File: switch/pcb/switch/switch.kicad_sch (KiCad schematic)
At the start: 29 parts, among them J1 Conn_01x02_Female, SW1 SW_MEC_5G, U1 LNK304D

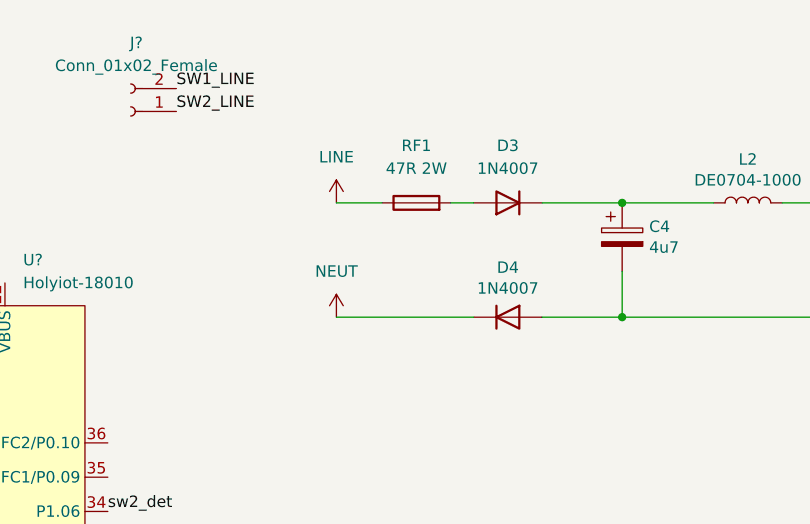
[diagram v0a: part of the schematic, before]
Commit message: switch: Add feature to set number of heartbeat pulses through CoAP
It is needed to disable heartbeats while debuggin hardware in production.
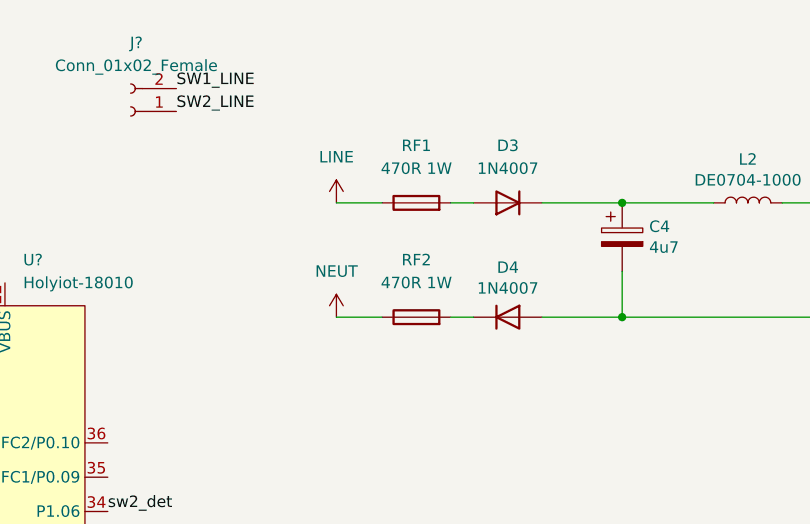
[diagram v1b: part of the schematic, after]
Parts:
- added RF2: 470R 1W, symbol Device:Fuse
- RF1: value 47R 2W -> 470R 1W
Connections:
- net NEUT: now also RF2.1; no longer D4.1 (K)
- new net: D4.1 (K), RF2.2

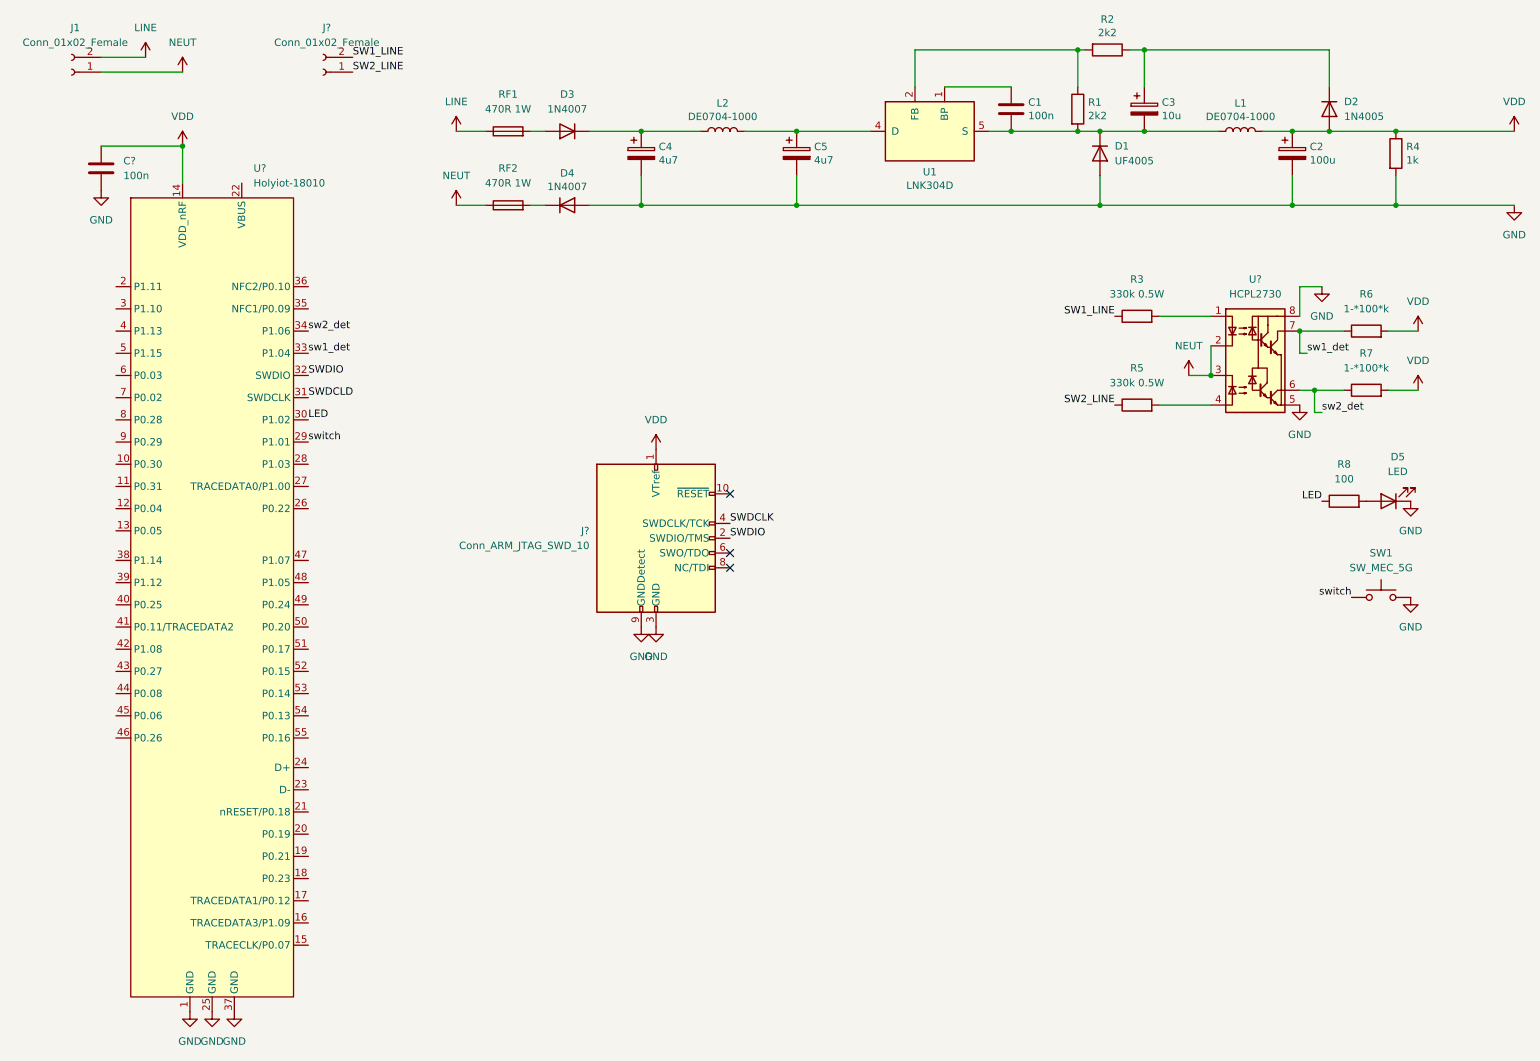
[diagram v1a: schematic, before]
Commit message: switch: Use ADC as an alternate switch detection
It looks some light switches do not disconnect electrical circuit but
increase their impedance instead. Impedance is low enough to keep
transoptor active, but with lower intensity than when the switch is
on. Transoptor intensity is detected with ADC and changes in intensity
treated as switch events.
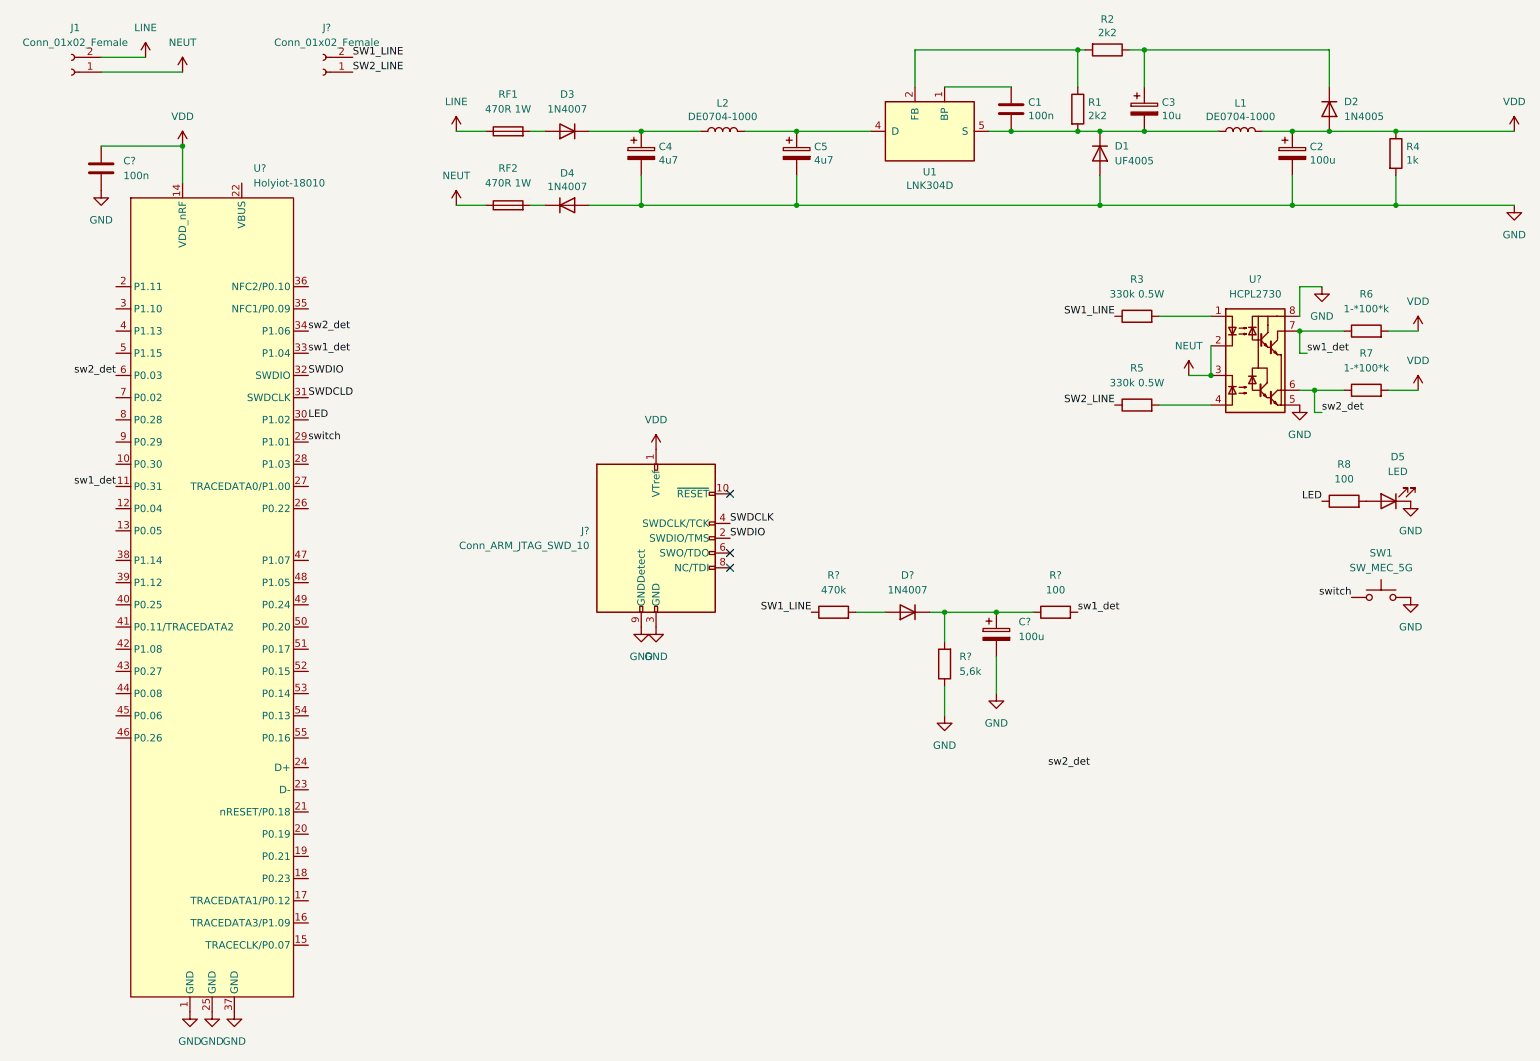
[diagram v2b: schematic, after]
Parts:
- added C?: 100u, symbol Device:C_Polarized
- added D?: 1N4007, symbol Device:D
- added R?: 5,6k, symbol Device:R
- added R?: 470k, symbol Device:R
- added R?: 100, symbol Device:R
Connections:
- net GND: now also C?.2, R?.1
- net SW1_LINE: now also R?.1
- net sw1_det: now also U?.11 (P0.31), R?.2
- net sw2_det: now also U?.6 (P0.03)
- new net: C?.1, D?.1 (K), R?.1, R?.2
- new net: D?.2 (A), R?.2
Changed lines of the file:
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@@
   (junction (at 252.73 36.83) (diameter 0) (color 0 0 0 0)
   )
+  (junction (at 175.26 119.38) (diameter 0) (color 0 0 0 0)
+  )
   (junction (at 201.93 36.83) (diameter 0) (color 0 0 0 0)
   )
@@
   )
   (junction (at 234.95 49.53) (diameter 0) (color 0 0 0 0)
+  )
+  (junction (at 184.15 119.38) (diameter 0) (color 0 0 0 0)
   )
   (junction (at 123.19 49.53) (diameter 0) (color 0 0 0 0)
@@
   (no_connect (at 138.43 111.76))
   (no_connect (at 138.43 109.22))
+  (wire (pts (xy 175.26 119.38) (xy 175.26 124.46))
+    (stroke (width 0) (type default) (color 0 0 0 0))
+  )
   (wire (pts (xy 240.03 85.09) (xy 238.76 85.09))
     (stroke (width 0) (type default) (color 0 0 0 0))
@@
     (stroke (width 0) (type default) (color 0 0 0 0))
   )
+  (wire (pts (xy 184.15 119.38) (xy 190.5 119.38))
+    (stroke (width 0) (type default) (color 0 0 0 0))
+  )
+  (wire (pts (xy 172.72 119.38) (xy 175.26 119.38))
+    (stroke (width 0) (type default) (color 0 0 0 0))
+  )
   (wire (pts (xy 234.95 36.83) (xy 241.3 36.83))
     (stroke (width 0) (type default) (color 0 0 0 0))
@@
     (stroke (width 0) (type default) (color 0 0 0 0))
   )
+  (wire (pts (xy 175.26 119.38) (xy 184.15 119.38))
+    (stroke (width 0) (type default) (color 0 0 0 0))
+  )
   (wire (pts (xy 252.73 36.83) (xy 273.05 36.83))
     (stroke (width 0) (type default) (color 0 0 0 0))
@@
     (stroke (width 0) (type default) (color 0 0 0 0))
   )
+  (wire (pts (xy 160.02 119.38) (xy 165.1 119.38))
+    (stroke (width 0) (type default) (color 0 0 0 0))
+  )
   (wire (pts (xy 186.69 36.83) (xy 198.12 36.83))
     (stroke (width 0) (type default) (color 0 0 0 0))
@@
     (stroke (width 0) (type default) (color 0 0 0 0))
   )
+  (wire (pts (xy 184.15 127) (xy 184.15 133.35))
+    (stroke (width 0) (type default) (color 0 0 0 0))
+  )
   (wire (pts (xy 234.95 44.45) (xy 234.95 49.53))
     (stroke (width 0) (type default) (color 0 0 0 0))
@@
     (stroke (width 0) (type default) (color 0 0 0 0))
   )
+  (wire (pts (xy 175.26 132.08) (xy 175.26 137.16))
+    (stroke (width 0) (type default) (color 0 0 0 0))
+  )
   (wire (pts (xy 114.3 49.53) (xy 123.19 49.53))
     (stroke (width 0) (type default) (color 0 0 0 0))
@@
   (wire (pts (xy 201.93 49.53) (xy 234.95 49.53))
     (stroke (width 0) (type default) (color 0 0 0 0))
+  )
+  (label "SW1_LINE" (at 152.4 119.38 180)
+    (effects (font (size 1.27 1.27)) (justify right bottom))
   )
   (label "SWDIO" (at 138.43 106.68 0)
     (effects (font (size 1.27 1.27)) (justify left bottom))
   )
+  (label "sw2_det" (at 193.04 146.05 0)
+    (effects (font (size 1.27 1.27)) (justify left bottom))
+  )
   (label "SW1_LINE" (at 204.47 68.58 180)
     (effects (font (size 1.27 1.27)) (justify right bottom))
@@
     (effects (font (size 1.27 1.27)) (justify left bottom))
   )
+  (label "sw2_det" (at 33.02 78.74 180)
+    (effects (font (size 1.27 1.27)) (justify right bottom))
+  )
   (label "sw1_det" (at 237.49 74.93 0)
     (effects (font (size 1.27 1.27)) (justify left bottom))
@@
     (effects (font (size 1.27 1.27)) (justify right bottom))
   )
+  (label "sw1_det" (at 33.02 97.79 180)
+    (effects (font (size 1.27 1.27)) (justify right bottom))
+  )
   (label "SW2_LINE" (at 204.47 83.82 180)
     (effects (font (size 1.27 1.27)) (justify right bottom))
+  )
+  (label "sw1_det" (at 198.12 119.38 0)
+    (effects (font (size 1.27 1.27)) (justify left bottom))
   )
   (label "switch" (at 66.04 90.17 0)
@@
     (pin "1")
   )
+  (symbol (lib_id "Device:D") (at 168.91 119.38 180) (unit 1)
+    (in_bom yes) (on_board yes) (fields_autoplaced)
+    (property "Reference" "D?" (id 0) (at 168.91 113.03 0))
+    (property "Value" "1N4007" (id 1) (at 168.91 115.57 0))
+    (property "Footprint" "" (id 2) (at 168.91 119.38 0)
+      (effects (font (size 1.27 1.27)) hide)
+    )
+    (property "Datasheet" "~" (id 3) (at 168.91 119.38 0)
+      (effects (font (size 1.27 1.27)) hide)
+    )
+    (pin "1")
+    (pin "2")
+  )
   (symbol (lib_id "Switch:SW_MEC_5G") (at 250.19 116.84 0) (unit 1)
     (in_bom yes) (on_board yes) (fields_autoplaced)
@@
     (pin "1")
   )
+  (symbol (lib_id "Device:R") (at 175.26 128.27 180) (unit 1)
+    (in_bom yes) (on_board yes) (fields_autoplaced)
+    (property "Reference" "R?" (id 0) (at 177.8 126.9999 0)
+      (effects (font (size 1.27 1.27)) (justify right))
+    )
+    (property "Value" "5,6k" (id 1) (at 177.8 129.5399 0)
+      (effects (font (size 1.27 1.27)) (justify right))
+    )
+    (property "Footprint" "" (id 2) (at 177.038 128.27 90)
+      (effects (font (size 1.27 1.27)) hide)
+    )
+    (property "Datasheet" "~" (id 3) (at 175.26 128.27 0)
+      (effects (font (size 1.27 1.27)) hide)
+    )
+    (pin "1")
+    (pin "2")
+  )
   (symbol (lib_id "Device:R") (at 208.28 68.58 90) (unit 1)
     (in_bom yes) (on_board yes) (fields_autoplaced)
@@
     )
     (property "Datasheet" "~" (id 3) (at 252.73 40.64 0)
+      (effects (font (size 1.27 1.27)) hide)
+    )
+    (pin "1")
+    (pin "2")
+  )
+  (symbol (lib_id "Device:C_Polarized") (at 184.15 123.19 0) (unit 1)
+    (in_bom yes) (on_board yes)
+    (property "Reference" "C?" (id 0) (at 187.96 121.0309 0)
+      (effects (font (size 1.27 1.27)) (justify left))
+    )
+    (property "Value" "100u" (id 1) (at 187.96 123.5709 0)
+      (effects (font (size 1.27 1.27)) (justify left))
+    )
+    (property "Footprint" "" (id 2) (at 185.1152 127 0)
+      (effects (font (size 1.27 1.27)) hide)
+    )
+    (property "Datasheet" "~" (id 3) (at 184.15 123.19 0)
       (effects (font (size 1.27 1.27)) hide)
     )
@@
     (pin "2")
   )
+  (symbol (lib_id "power:GND") (at 184.15 133.35 0) (unit 1)
+    (in_bom yes) (on_board yes)
+    (property "Reference" "#PWR?" (id 0) (at 184.15 139.7 0)
+      (effects (font (size 1.27 1.27)) hide)
+    )
+    (property "Value" "GND" (id 1) (at 184.15 138.43 0))
+    (property "Footprint" "" (id 2) (at 184.15 133.35 0)
+      (effects (font (size 1.27 1.27)) hide)
+    )
+    (property "Datasheet" "" (id 3) (at 184.15 133.35 0)
+      (effects (font (size 1.27 1.27)) hide)
+    )
+    (pin "1")
+  )
   (symbol (lib_id "Device:LED") (at 251.46 100.33 180) (unit 1)
     (in_bom yes) (on_board yes) (fields_autoplaced)
@@
     (pin "2")
   )
+  (symbol (lib_id "power:GND") (at 175.26 137.16 0) (unit 1)
+    (in_bom yes) (on_board yes)
+    (property "Reference" "#PWR?" (id 0) (at 175.26 143.51 0)
+      (effects (font (size 1.27 1.27)) hide)
+    )
+    (property "Value" "GND" (id 1) (at 175.26 142.24 0))
+    (property "Footprint" "" (id 2) (at 175.26 137.16 0)
+      (effects (font (size 1.27 1.27)) hide)
+    )
+    (property "Datasheet" "" (id 3) (at 175.26 137.16 0)
+      (effects (font (size 1.27 1.27)) hide)
+    )
+    (pin "1")
+  )
   (symbol (lib_id "Device:D") (at 201.93 40.64 270) (unit 1)
     (in_bom yes) (on_board yes) (fields_autoplaced)
@@
     )
     (pin "1")
+  )
+  (symbol (lib_id "Device:R") (at 156.21 119.38 90) (unit 1)
+    (in_bom yes) (on_board yes) (fields_autoplaced)
+    (property "Reference" "R?" (id 0) (at 156.21 113.03 90))
+    (property "Value" "470k" (id 1) (at 156.21 115.57 90))
+    (property "Footprint" "" (id 2) (at 156.21 121.158 90)
+      (effects (font (size 1.27 1.27)) hide)
+    )
+    (property "Datasheet" "~" (id 3) (at 156.21 119.38 0)
+      (effects (font (size 1.27 1.27)) hide)
+    )
+    (pin "1")
+    (pin "2")
+  )
+  (symbol (lib_id "Device:R") (at 194.31 119.38 90) (unit 1)
+    (in_bom yes) (on_board yes) (fields_autoplaced)
+    (property "Reference" "R?" (id 0) (at 194.31 113.03 90))
+    (property "Value" "100" (id 1) (at 194.31 115.57 90))
+    (property "Footprint" "" (id 2) (at 194.31 121.158 90)
+      (effects (font (size 1.27 1.27)) hide)
+    )
+    (property "Datasheet" "~" (id 3) (at 194.31 119.38 0)
+      (effects (font (size 1.27 1.27)) hide)
+    )
+    (pin "1")
+    (pin "2")
   )
   (symbol (lib_id "Device:L") (at 137.16 36.83 90) (unit 1)
@@
       (reference "#PWR0121") (unit 1) (value "GND") (footprint "")
     )
+    (path "/87fbc6e1-d9f2-456e-87f8-64a6ecae251a"
+      (reference "#PWR?") (unit 1) (value "GND") (footprint "")
+    )
+    (path "/922a768b-0e27-4961-9614-65b6bb3f04e1"
+      (reference "#PWR?") (unit 1) (value "GND") (footprint "")
+    )
     (path "/00000000-0000-0000-0000-000061918be5"
       (reference "C1") (unit 1) (value "100n") (footprint "")
@@
       (reference "C?") (unit 1) (value "100n") (footprint "")
     )
+    (path "/4b115909-f3b8-4ccb-bfb8-ebcf57908398"
+      (reference "C?") (unit 1) (value "100u") (footprint "")
+    )
     (path "/94fd1f74-d65f-4867-99b9-45c8691b542a"
       (reference "D1") (unit 1) (value "UF4005") (footprint "")
@@
       (reference "D5") (unit 1) (value "LED") (footprint "")
     )
+    (path "/18322203-88aa-46cc-b836-30d2ae1d104e"
+      (reference "D?") (unit 1) (value "1N4007") (footprint "")
+    )
     (path "/762eaf6c-5998-491d-81d0-e246116e9d79"
       (reference "J1") (unit 1) (value "Conn_01x02_Female") (footprint "")
@@
       (reference "R8") (unit 1) (value "100") (footprint "")
     )
+    (path "/33410be8-f39b-40fd-a6fc-2ddb93cb41dd"
+      (reference "R?") (unit 1) (value "5,6k") (footprint "")
+    )
+    (path "/9d1eced5-7e55-4529-8e92-a46f2c4c3bfa"
+      (reference "R?") (unit 1) (value "470k") (footprint "")
+    )
+    (path "/a14b858d-a42c-4f8a-aa4e-2e161be8060d"
+      (reference "R?") (unit 1) (value "100") (footprint "")
+    )
     (path "/c312d95f-a24d-40b1-9fa0-0b88368031dc"
